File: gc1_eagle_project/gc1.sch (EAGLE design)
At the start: 9 parts

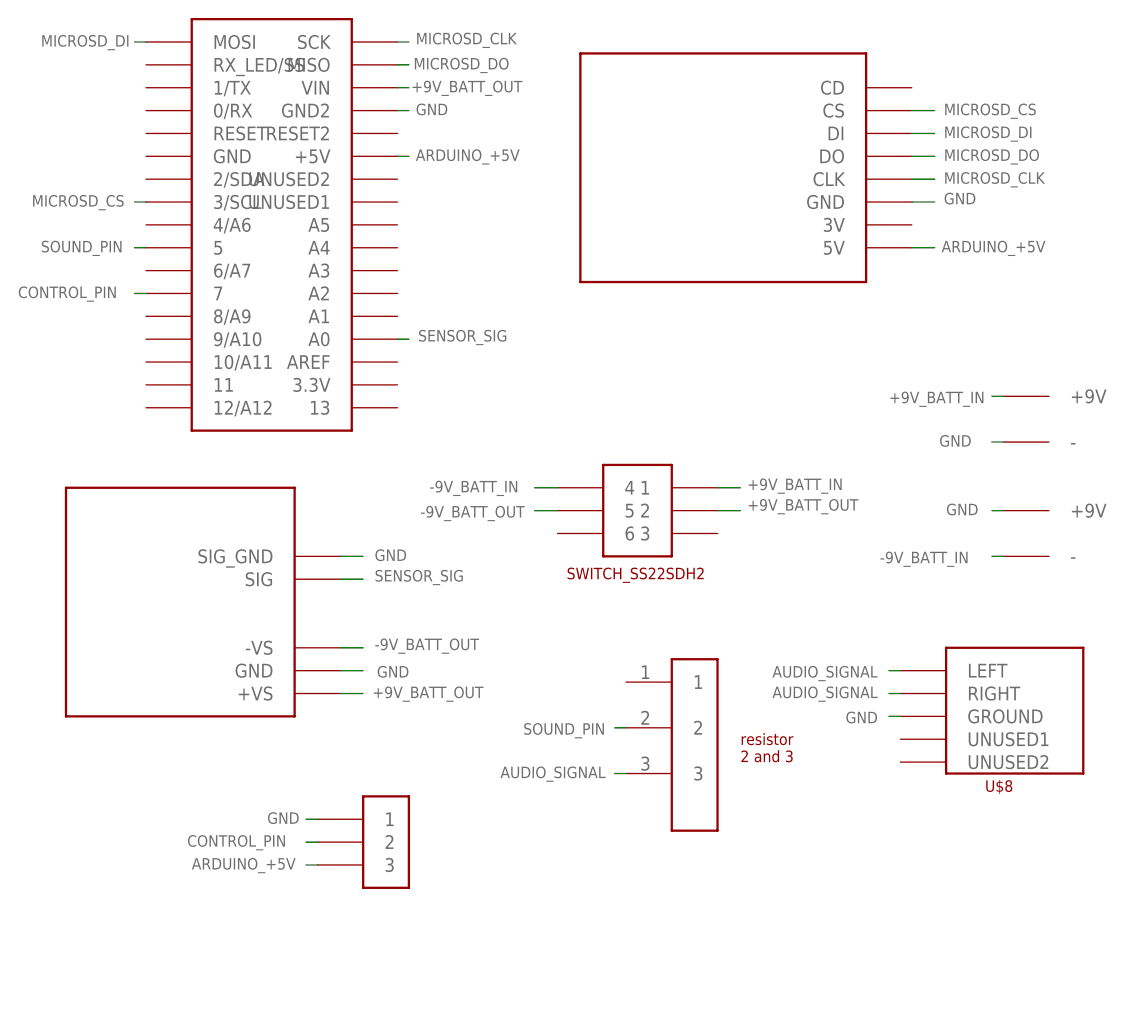
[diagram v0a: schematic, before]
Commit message: swapped some parts, added 10k resistor between arduino 5v and control pin
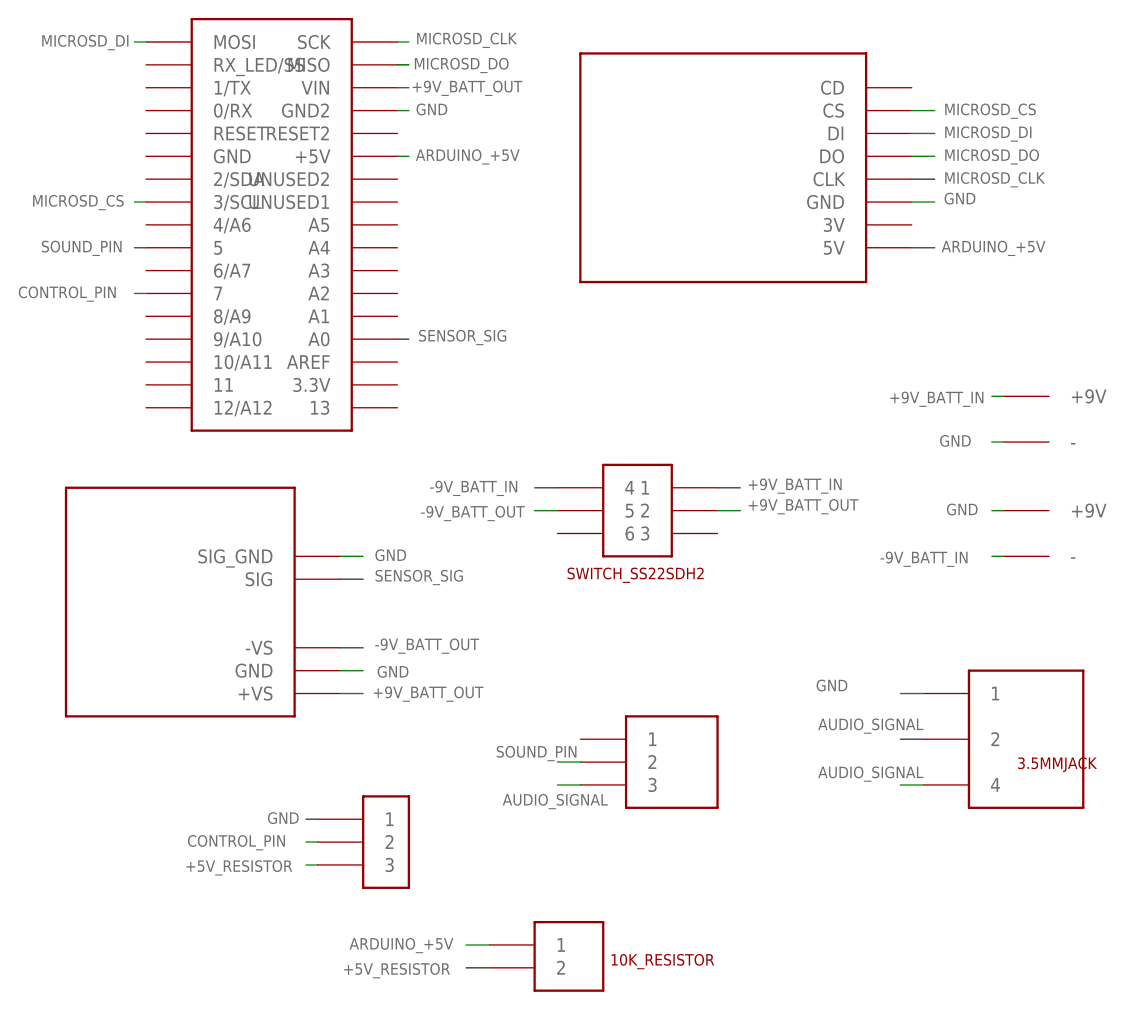
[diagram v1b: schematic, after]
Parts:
- removed U$7: TRIMPOT_3006, gc1_parts:TRIMPOT_3006
- removed U$8: STEREOJACK_35RAPC2BHN2, gc1_parts:STEREOJACK_35RAPC2BHN2
- added 10K_RESISTOR: 10K_RESISTOR, gc1_parts:10K_RESISTOR
- added 3.5MMJACK: 35RAPC2BVN4, gc1_parts:35RAPC2BVN4
- added TRIMMER: 66WR1KLF, gc1_parts:66WR1KLF
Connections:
- new net +5V_RESISTOR: 10K_RESISTOR.2, U$9.3
- net ARDUINO_+5V: now also 10K_RESISTOR.1; no longer U$9.3
- net AUDIO_SIGNAL: now also 3.5MMJACK.2, 3.5MMJACK.4, TRIMMER.3; no longer U$7.3, U$8.LEFT, U$8.RIGHT
- net GND: now also 3.5MMJACK.1; no longer U$8.GROUND
- net SOUND_PIN: now also TRIMMER.2; no longer U$7.2
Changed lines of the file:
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@@
 </variantdefs>
 <classes>
-<class number="0" name="default" width="0" drill="0">
+<class number="0" name="default" width="0.6096" drill="0">
 </class>
 </classes>
@@
 <part name="U$5" library="gc1_parts" deviceset="9V_CONNECTOR" device=""/>
 <part name="U$6" library="gc1_parts" deviceset="9V_CONNECTOR" device=""/>
-<part name="U$7" library="gc1_parts" deviceset="TRIMPOT_3006" device=""/>
-<part name="U$8" library="gc1_parts" deviceset="STEREOJACK_35RAPC2BHN2" device=""/>
 <part name="U$9" library="gc1_parts" deviceset="SWITCH_SS12SDH2" device=""/>
+<part name="3.5MMJACK" library="gc1_parts" deviceset="35RAPC2BVN4" device=""/>
+<part name="TRIMMER" library="gc1_parts" deviceset="66WR1KLF" device=""/>
+<part name="10K_RESISTOR" library="gc1_parts" deviceset="10K_RESISTOR" device=""/>
 </parts>
 <sheets>
@@
 <instance part="U$5" gate="G$1" x="97.79" y="-43.18"/>
 <instance part="U$6" gate="G$1" x="97.79" y="-55.88"/>
-<instance part="U$7" gate="G$1" x="63.5" y="-67.31"/>
-<instance part="U$8" gate="G$1" x="101.6" y="-72.39"/>
 <instance part="U$9" gate="G$1" x="29.21" y="-82.55"/>
+<instance part="3.5MMJACK" gate="G$1" x="101.6" y="-76.2"/>
+<instance part="TRIMMER" gate="G$1" x="58.42" y="-78.74"/>
+<instance part="10K_RESISTOR" gate="G$1" x="48.26" y="-99.06"/>
 </instances>
 <busses>
@@
 </segment>
 <segment>
-<pinref part="U$9" gate="G$1" pin="3"/>
-<wire x1="24.13" y1="-90.17" x2="22.86" y2="-90.17" width="0.1524" layer="91"/>
-<label x="10.16" y="-90.678" size="1.27" layer="95"/>
+<pinref part="10K_RESISTOR" gate="G$1" pin="1"/>
+<wire x1="43.18" y1="-99.06" x2="40.64" y2="-99.06" width="0.1524" layer="91"/>
+<label x="27.686" y="-99.568" size="1.27" layer="95"/>
 </segment>
 </net>
@@
 </segment>
 <segment>
-<pinref part="U$8" gate="G$1" pin="GROUND"/>
-<wire x1="88.9" y1="-73.66" x2="87.63" y2="-73.66" width="0.1524" layer="91"/>
-<label x="82.804" y="-74.422" size="1.27" layer="95"/>
-</segment>
-<segment>
 <pinref part="U$9" gate="G$1" pin="1"/>
 <wire x1="24.13" y1="-85.09" x2="22.86" y2="-85.09" width="0.1524" layer="91"/>
 <label x="18.542" y="-85.598" size="1.27" layer="95"/>
 </segment>
+<segment>
+<pinref part="3.5MMJACK" gate="G$1" pin="1"/>
+<wire x1="91.44" y1="-71.12" x2="88.9" y2="-71.12" width="0.1524" layer="91"/>
+<label x="79.502" y="-70.866" size="1.27" layer="95"/>
+</segment>
 </net>
 <net name="MICROSD_CS" class="0">
@@
 </segment>
 <segment>
-<pinref part="U$7" gate="G$1" pin="2"/>
-<wire x1="58.42" y1="-74.93" x2="57.15" y2="-74.93" width="0.1524" layer="91"/>
-<label x="46.99" y="-75.692" size="1.27" layer="95"/>
+<pinref part="TRIMMER" gate="G$1" pin="2"/>
+<wire x1="53.34" y1="-78.74" x2="50.8" y2="-78.74" width="0.1524" layer="91"/>
+<label x="43.942" y="-78.232" size="1.27" layer="95"/>
 </segment>
 </net>
 <net name="AUDIO_SIGNAL" class="0">
 <segment>
-<pinref part="U$7" gate="G$1" pin="3"/>
-<wire x1="58.42" y1="-80.01" x2="57.15" y2="-80.01" width="0.1524" layer="91"/>
-<label x="44.45" y="-80.518" size="1.27" layer="95"/>
-</segment>
-<segment>
-<pinref part="U$8" gate="G$1" pin="LEFT"/>
-<wire x1="88.9" y1="-68.58" x2="87.63" y2="-68.58" width="0.1524" layer="91"/>
-<label x="74.676" y="-69.342" size="1.27" layer="95"/>
-</segment>
-<segment>
-<pinref part="U$8" gate="G$1" pin="RIGHT"/>
-<wire x1="88.9" y1="-71.12" x2="87.63" y2="-71.12" width="0.1524" layer="91"/>
-<label x="74.676" y="-71.628" size="1.27" layer="95"/>
+<pinref part="3.5MMJACK" gate="G$1" pin="2"/>
+<wire x1="91.44" y1="-76.2" x2="88.9" y2="-76.2" width="0.1524" layer="91"/>
+<label x="79.756" y="-75.184" size="1.27" layer="95"/>
+</segment>
+<segment>
+<pinref part="TRIMMER" gate="G$1" pin="3"/>
+<wire x1="53.34" y1="-81.28" x2="50.8" y2="-81.28" width="0.1524" layer="91"/>
+<label x="44.704" y="-83.566" size="1.27" layer="95"/>
+</segment>
+<segment>
+<pinref part="3.5MMJACK" gate="G$1" pin="4"/>
+<wire x1="91.44" y1="-81.28" x2="88.9" y2="-81.28" width="0.1524" layer="91"/>
+<label x="79.756" y="-80.518" size="1.27" layer="95"/>
 </segment>
 </net>
@@
 <wire x1="24.13" y1="-87.63" x2="22.86" y2="-87.63" width="0.1524" layer="91"/>
 <label x="9.652" y="-88.138" size="1.27" layer="95"/>
+</segment>
+</net>
+<net name="+5V_RESISTOR" class="0">
+<segment>
+<pinref part="10K_RESISTOR" gate="G$1" pin="2"/>
+<wire x1="43.18" y1="-101.6" x2="40.64" y2="-101.6" width="0.1524" layer="91"/>
+<label x="26.924" y="-102.362" size="1.27" layer="95"/>
+</segment>
+<segment>
+<pinref part="U$9" gate="G$1" pin="3"/>
+<wire x1="24.13" y1="-90.17" x2="22.86" y2="-90.17" width="0.1524" layer="91"/>
+<label x="9.398" y="-90.932" size="1.27" layer="95"/>
 </segment>
 </net>
@@
 </schematic>
 </drawing>
-<compatibility>
-<note version="6.3" minversion="6.2.2" severity="warning">
-Since Version 6.2.2 text objects can contain more than one line,
-which will not be processed correctly with this version.
-</note>
-</compatibility>
 </eagle>
